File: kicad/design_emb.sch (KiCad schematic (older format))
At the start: 3 parts, among them J1 Conn_01x03, U1 SRX.X.TCT, U2 SRX.X.TCT

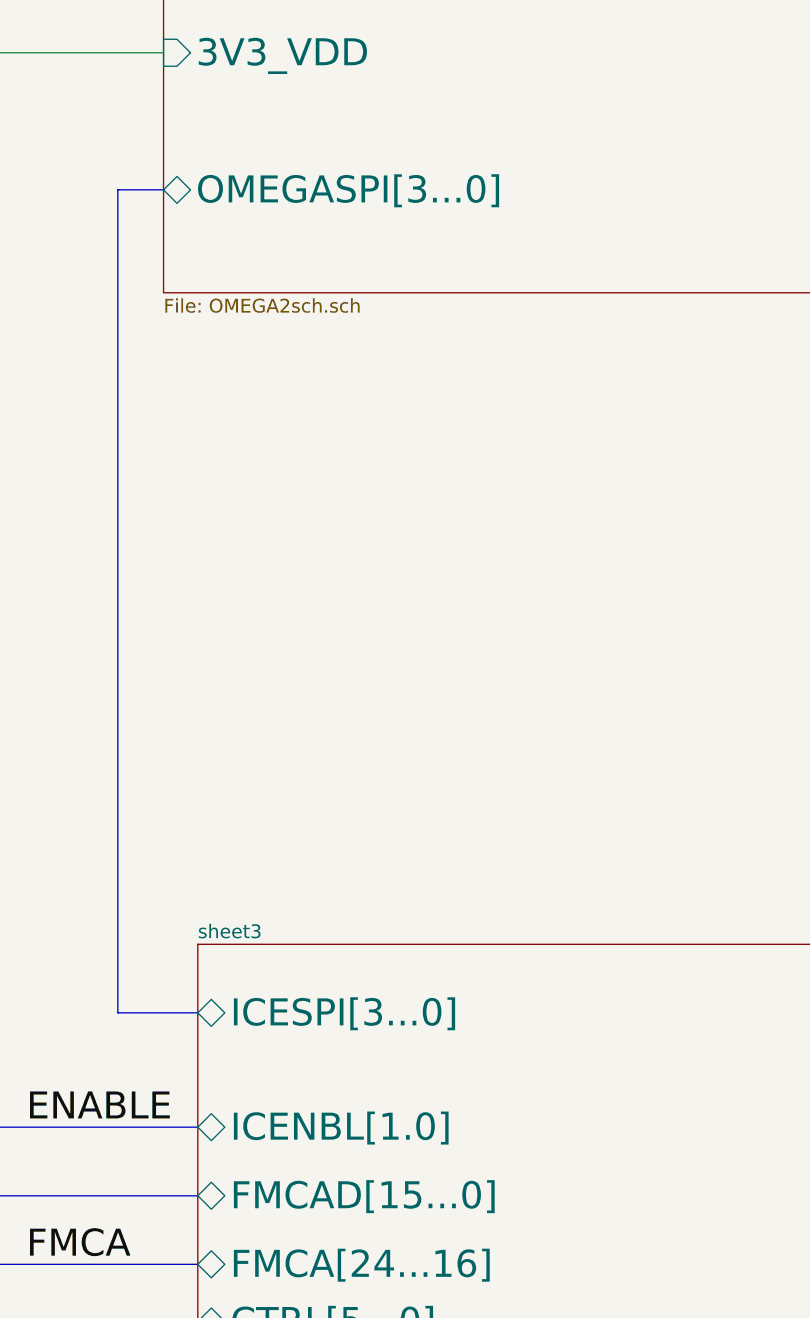
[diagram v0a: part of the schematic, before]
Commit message: arreglo pines FPGA compatibilidad STM32
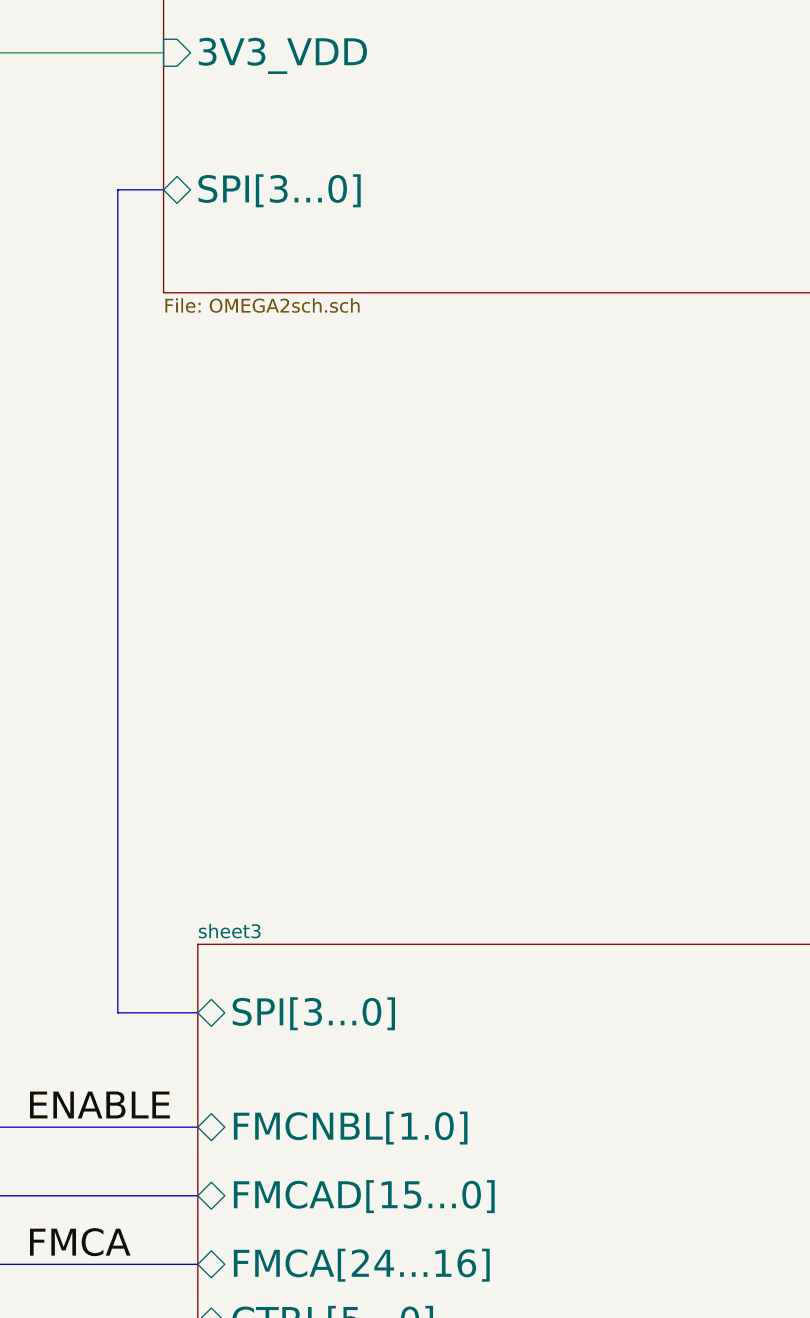
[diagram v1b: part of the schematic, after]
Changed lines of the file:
@@
 EESchema Schematic File Version 4
+LIBS:power
+LIBS:74xx
 LIBS:stm32f446zetx
 LIBS:design_emb-cache
@@
 F2 "FMCAD[15...0]" B L 30050 18150 118
 F3 "FMCA[24...16]" B L 30050 18450 118
-F4 "ICENBL[1.0]" B L 30050 17850 118
-F5 "ICESPI[3...0]" B L 30050 17350 118
+F4 "FMCNBL[1.0]" B L 30050 17850 118
+F5 "SPI[3...0]" B L 30050 17350 118
 F6 "CTRL[5...0]" B L 30050 18700 118
 F7 "+1V2_FPGA" I L 30050 23050 118
@@
 F5 "UART_RX" I L 29900 7300 118
 F6 "UART_TX" O L 29900 7550 118
-F7 "OMEGASPI[3...0]" B L 29900 13750 118
+F7 "SPI[3...0]" B L 29900 13750 118
 F8 "JTAG[5...0]" B L 29900 8700 118
 F9 "BOOT0" O L 29900 8950 118

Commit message: ruteo
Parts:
- removed J1: Conn_01x03, Connectors_Terminal_Blocks:TerminalBlock_Altech_AK300-3_P5.00mm, symbol conn:Conn_01x03
- added J1: Conn_01x04, Connector_PinSocket_2.54mm:PinSocket_1x04_P2.54mm_Horizontal, symbol conn:Conn_01x04
- added L4, L5: L, Inductors_SMD:L_0805_HandSoldering, symbol Device:L
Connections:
- net labels added: 3V3_O
- wire segments 30 -> 33
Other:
- note added: "OWL_BOARD 1.0"
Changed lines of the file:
@@
 encoding utf-8
 Sheet 1 6
-Title ""
+Title "OWL_BOARD 1.0"
 Date ""
 Rev ""
-Comp ""
-Comment1 ""
-Comment2 ""
+Comp "Fabio Segura y Freddy Vanegas"
+Comment1 "de la Maestría en Ingeniería Electrónica de la Universidad Nacional de Colombia"
+Comment2 "Tarjeta diseñada para la asiganatura \"Diseño e implementación de sistemas embebidos\""
 Comment3 ""
 Comment4 ""
@@
 L ESD_Protection:SRX.X.TCT U?
 U 1 1 5B9A3C31
-P 41100 3350
+P 40900 7250
 AR Path="/5B7D9546/5B9A3C31" Ref="U?"  Part="1"
 AR Path="/5B9A3C31" Ref="U1"  Part="1"
-F 0 "U1" H 41000 3150 60  0000 C CNN
-F 1 "SRX.X.TCT" H 41100 3591 60  0000 C CNN
-F 2 "TO_SOT_Packages_SMD:SOT-143" H 41100 3350 60  0001 C CNN
-F 3 "https://co.mouser.com/datasheet/2/761/sr2_8-1277654.pdf" H 41100 3350 60  0001 C CNN
-	1    41100 3350
+F 0 "U1" H 40800 7050 60  0000 C CNN
+F 1 "SRX.X.TCT" H 40900 7491 60  0000 C CNN
+F 2 "TO_SOT_Packages_SMD:SOT-143" H 40900 7250 60  0001 C CNN
+F 3 "https://co.mouser.com/datasheet/2/761/sr2_8-1277654.pdf" H 40900 7250 60  0001 C CNN
+	1    40900 7250
 	1    0    0    -1
 $EndComp
 Wire Wire Line
-	40800 3250 40700 3250
+	40600 7150 40500 7150
 $Comp
 L power:GND #PWR?
 U 1 1 5B9A3C39
-P 40700 3250
+P 40500 7150
 AR Path="/5B7D9546/5B9A3C39" Ref="#PWR?"  Part="1"
 AR Path="/5B9A3C39" Ref="#PWR01"  Part="1"
-F 0 "#PWR01" H 40700 3000 50  0001 C CNN
-F 1 "GND" V 40705 3122 50  0000 R CNN
-F 2 "" H 40700 3250 50  0001 C CNN
-F 3 "" H 40700 3250 50  0001 C CNN
-	1    40700 3250
+F 0 "#PWR01" H 40500 6900 50  0001 C CNN
+F 1 "GND" V 40505 7022 50  0000 R CNN
+F 2 "" H 40500 7150 50  0001 C CNN
+F 3 "" H 40500 7150 50  0001 C CNN
+	1    40500 7150
 	0    1    1    0
 $EndComp
 Wire Wire Line
-	40800 3450 40250 3450
+	40600 7350 40050 7350
 $Comp
 L ESD_Protection:SRX.X.TCT U?
 U 1 1 5B9A3C41
-P 41100 3900
+P 40900 7800
 AR Path="/5B7D9546/5B9A3C41" Ref="U?"  Part="1"
 AR Path="/5B9A3C41" Ref="U2"  Part="1"
-F 0 "U2" H 41000 3700 60  0000 C CNN
-F 1 "SRX.X.TCT" H 41100 4141 60  0000 C CNN
-F 2 "TO_SOT_Packages_SMD:SOT-143" H 41100 3900 60  0001 C CNN
-F 3 "https://co.mouser.com/datasheet/2/761/sr2_8-1277654.pdf" H 41100 3900 60  0001 C CNN
-	1    41100 3900
+F 0 "U2" H 40800 7600 60  0000 C CNN
+F 1 "SRX.X.TCT" H 40900 8041 60  0000 C CNN
+F 2 "TO_SOT_Packages_SMD:SOT-143" H 40900 7800 60  0001 C CNN
+F 3 "https://co.mouser.com/datasheet/2/761/sr2_8-1277654.pdf" H 40900 7800 60  0001 C CNN
+	1    40900 7800
 	1    0    0    -1
 $EndComp
 Wire Wire Line
-	40800 3800 40700 3800
+	40600 7700 40500 7700
 $Comp
 L power:GND #PWR?
 U 1 1 5B9A3C49
-P 40700 3800
+P 40500 7700
 AR Path="/5B7D9546/5B9A3C49" Ref="#PWR?"  Part="1"
 AR Path="/5B9A3C49" Ref="#PWR02"  Part="1"
-F 0 "#PWR02" H 40700 3550 50  0001 C CNN
-F 1 "GND" V 40705 3672 50  0000 R CNN
-F 2 "" H 40700 3800 50  0001 C CNN
-F 3 "" H 40700 3800 50  0001 C CNN
-	1    40700 3800
+F 0 "#PWR02" H 40500 7450 50  0001 C CNN
+F 1 "GND" V 40505 7572 50  0000 R CNN
+F 2 "" H 40500 7700 50  0001 C CNN
+F 3 "" H 40500 7700 50  0001 C CNN
+	1    40500 7700
 	0    1    1    0
 $EndComp
 Wire Wire Line
-	40800 4000 40250 4000
-NoConn ~ 41400 3250
-NoConn ~ 41400 3800
-Wire Wire Line
-	42200 3450 41400 3450
-Wire Wire Line
-	42200 3550 41500 3550
-Wire Wire Line
-	41500 3550 41500 4000
-Wire Wire Line
-	41500 4000 41400 4000
-Text Label 42050 3450 2    60   ~ 0
+	40600 7900 40050 7900
+NoConn ~ 41200 7150
+NoConn ~ 41200 7700
+Wire Wire Line
+	42000 7350 41200 7350
+Wire Wire Line
+	42000 7450 41300 7450
+Wire Wire Line
+	41300 7450 41300 7900
+Wire Wire Line
+	41300 7900 41200 7900
+Text Label 41850 7350 2    60   ~ 0
 RX_OUT
-Text Label 42000 3550 2    60   ~ 0
+Text Label 41800 7450 2    60   ~ 0
 TX_IN
 Wire Wire Line
-	42200 3650 42100 3650
-Wire Wire Line
-	42100 3650 42100 3850
+	41700 7650 41600 7650
+Wire Wire Line
+	41600 7650 41600 7850
 $Comp
 L power:GND #PWR?
 U 1 1 5B9A3C62
-P 42100 3850
+P 41600 7850
 AR Path="/5B7D9546/5B9A3C62" Ref="#PWR?"  Part="1"
 AR Path="/5B9A3C62" Ref="#PWR03"  Part="1"
-F 0 "#PWR03" H 42100 3600 50  0001 C CNN
-F 1 "GND" H 42105 3677 50  0000 C CNN
-F 2 "" H 42100 3850 50  0001 C CNN
-F 3 "" H 42100 3850 50  0001 C CNN
-	1    42100 3850
+F 0 "#PWR03" H 41600 7600 50  0001 C CNN
+F 1 "GND" H 41605 7677 50  0000 C CNN
+F 2 "" H 41600 7850 50  0001 C CNN
+F 3 "" H 41600 7850 50  0001 C CNN
+	1    41600 7850
 	1    0    0    -1
 $EndComp
-Text Notes 43350 2850 2    197  Italic 0
+Text Notes 43150 6750 2    197  Italic 0
 User serial communication\n\n
-Text Notes 41950 4400 2    98   ~ 0
+Text Notes 41750 8300 2    98   ~ 0
 SR3.3.TCT / SR2.8.TCT
 $Sheet
@@
 F8 "JTAG[5...0]" B L 29900 8700 118
 F9 "BOOT0" O L 29900 8950 118
+F10 "V3.3OUT" I R 35100 7850 118
 $EndSheet
 Wire Wire Line
@@
 Wire Wire Line
 	26600 7550 26600 8150
-Text Label 40300 3450 0    60   ~ 0
+Text Label 40100 7350 0    60   ~ 0
 SERIAL_RX
-Text Label 40300 4000 0    60   ~ 0
+Text Label 40100 7900 0    60   ~ 0
 SERIAL_TX
 Wire Wire Line
@@
 Text Label 35150 7550 0    60   ~ 0
 SERIAL_TX
-$Comp
-L conn:Conn_01x03 J?
-U 1 1 5B9A3C53
-P 42400 3550
-AR Path="/5B7D9546/5B9A3C53" Ref="J?"  Part="1"
-AR Path="/5B9A3C53" Ref="J1"  Part="1"
-F 0 "J1" H 42480 3592 50  0000 L CNN
-F 1 "Conn_01x03" H 42480 3501 50  0000 L CNN
-F 2 "Connectors_Terminal_Blocks:TerminalBlock_Altech_AK300-3_P5.00mm" H 42400 3550 50  0001 C CNN
-F 3 "~" H 42400 3550 50  0001 C CNN
-	1    42400 3550
-	1    0    0    -1
-$EndComp
 Wire Wire Line
 	29900 13150 29100 13150
@@
 Wire Bus Line
 	22950 14400 26300 14400
+Text Notes 1450 1850 0    591  ~ 118
+OWL_BOARD 1.0
+$Comp
+L conn:Conn_01x04 J1
+U 1 1 5BC4E2DD
+P 42200 7450
+F 0 "J1" H 42280 7442 50  0000 L CNN
+F 1 "Conn_01x04" H 42280 7351 50  0000 L CNN
+F 2 "Connector_PinSocket_2.54mm:PinSocket_1x04_P2.54mm_Horizontal" H 42200 7450 50  0001 C CNN
+F 3 "~" H 42200 7450 50  0001 C CNN
+	1    42200 7450
+	1    0    0    -1
+$EndComp
+$Comp
+L Device:L L5
+U 1 1 5BC4EA09
+P 41850 7650
+F 0 "L5" V 41672 7650 50  0000 C CNN
+F 1 "L" V 41763 7650 50  0000 C CNN
+F 2 "Inductors_SMD:L_0805_HandSoldering" H 41850 7650 50  0001 C CNN
+F 3 "~" H 41850 7650 50  0001 C CNN
+	1    41850 7650
+	0    1    1    0
+$EndComp
+Wire Wire Line
+	35100 7850 35650 7850
+Text Label 35250 7850 0    59   ~ 0
+3V3_O
+Wire Wire Line
+	41500 7900 41500 7550
+Text Label 41500 7850 1    59   ~ 0
+3V3_O
+$Comp
+L Device:L L4
+U 1 1 5BC515BF
+P 41850 7550
+F 0 "L4" V 41672 7550 50  0000 C CNN
+F 1 "L" V 41763 7550 50  0000 C CNN
+F 2 "Inductors_SMD:L_0805_HandSoldering" H 41850 7550 50  0001 C CNN
+F 3 "~" H 41850 7550 50  0001 C CNN
+	1    41850 7550
+	0    1    1    0
+$EndComp
+Wire Wire Line
+	41700 7550 41500 7550
 $EndSCHEMATC

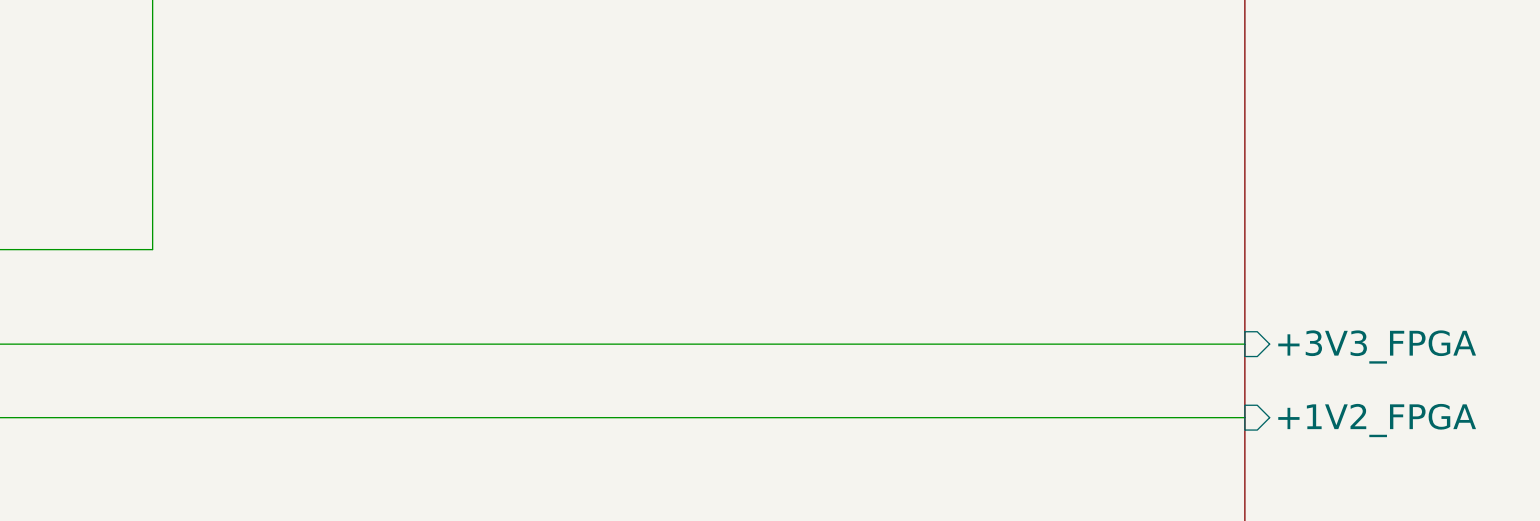
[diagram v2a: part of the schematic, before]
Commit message: plano de tierra y modificación de señales
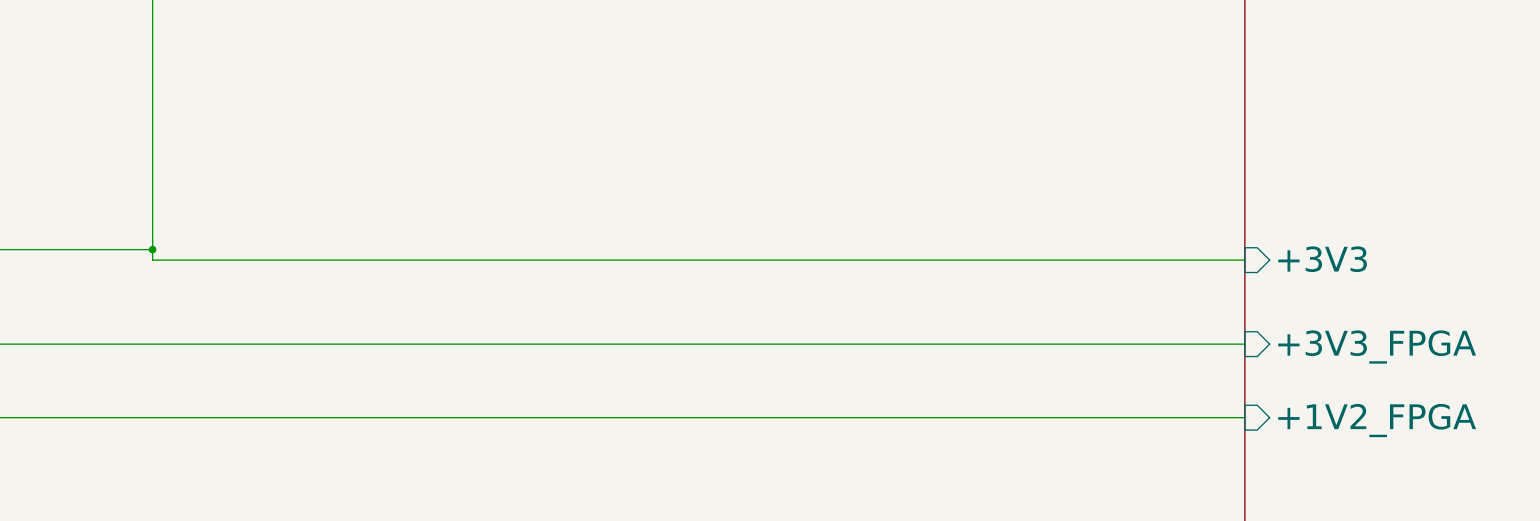
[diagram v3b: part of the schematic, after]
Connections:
- wire segments 33 -> 35
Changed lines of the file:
@@
 F7 "+1V2_FPGA" I L 30050 23050 118
 F8 "+3V3_FPGA" I L 30050 22700 118
+F9 "+3V3" I L 30050 22300 118
 $EndSheet
 $Sheet
@@
 Wire Wire Line
 	41700 7550 41500 7550
+Wire Wire Line
+	30050 22300 24850 22300
+Wire Wire Line
+	24850 22300 24850 22250
+Connection ~ 24850 22250
 $EndSCHEMATC
